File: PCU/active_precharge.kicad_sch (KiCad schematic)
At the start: 0 parts

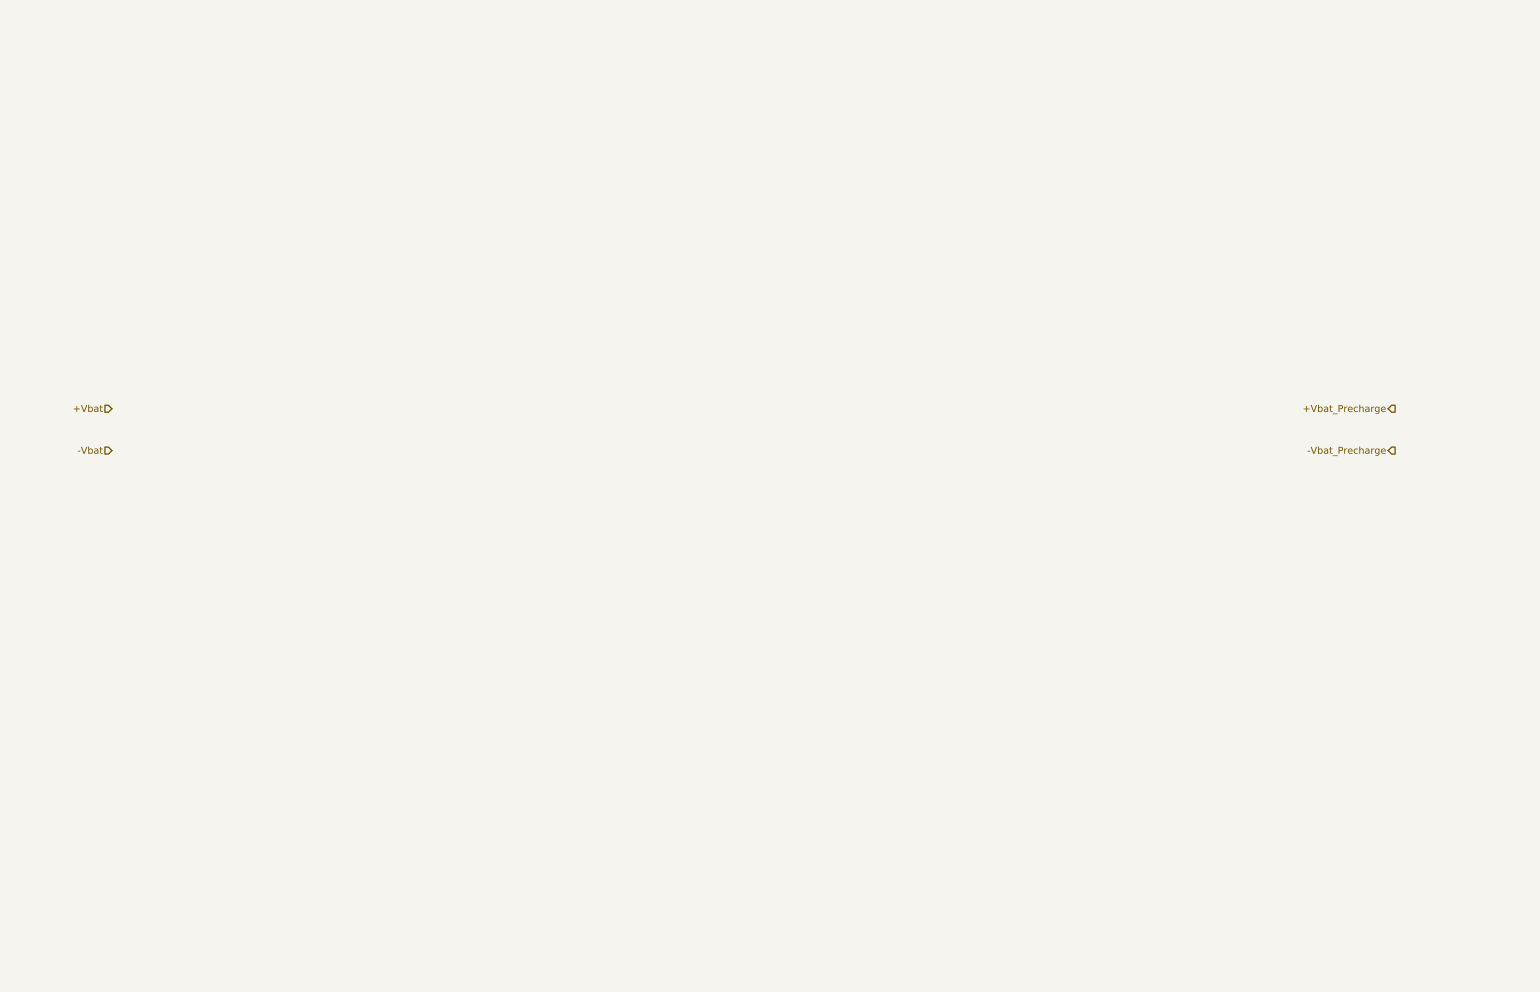
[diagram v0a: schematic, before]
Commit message: Active precharge Block
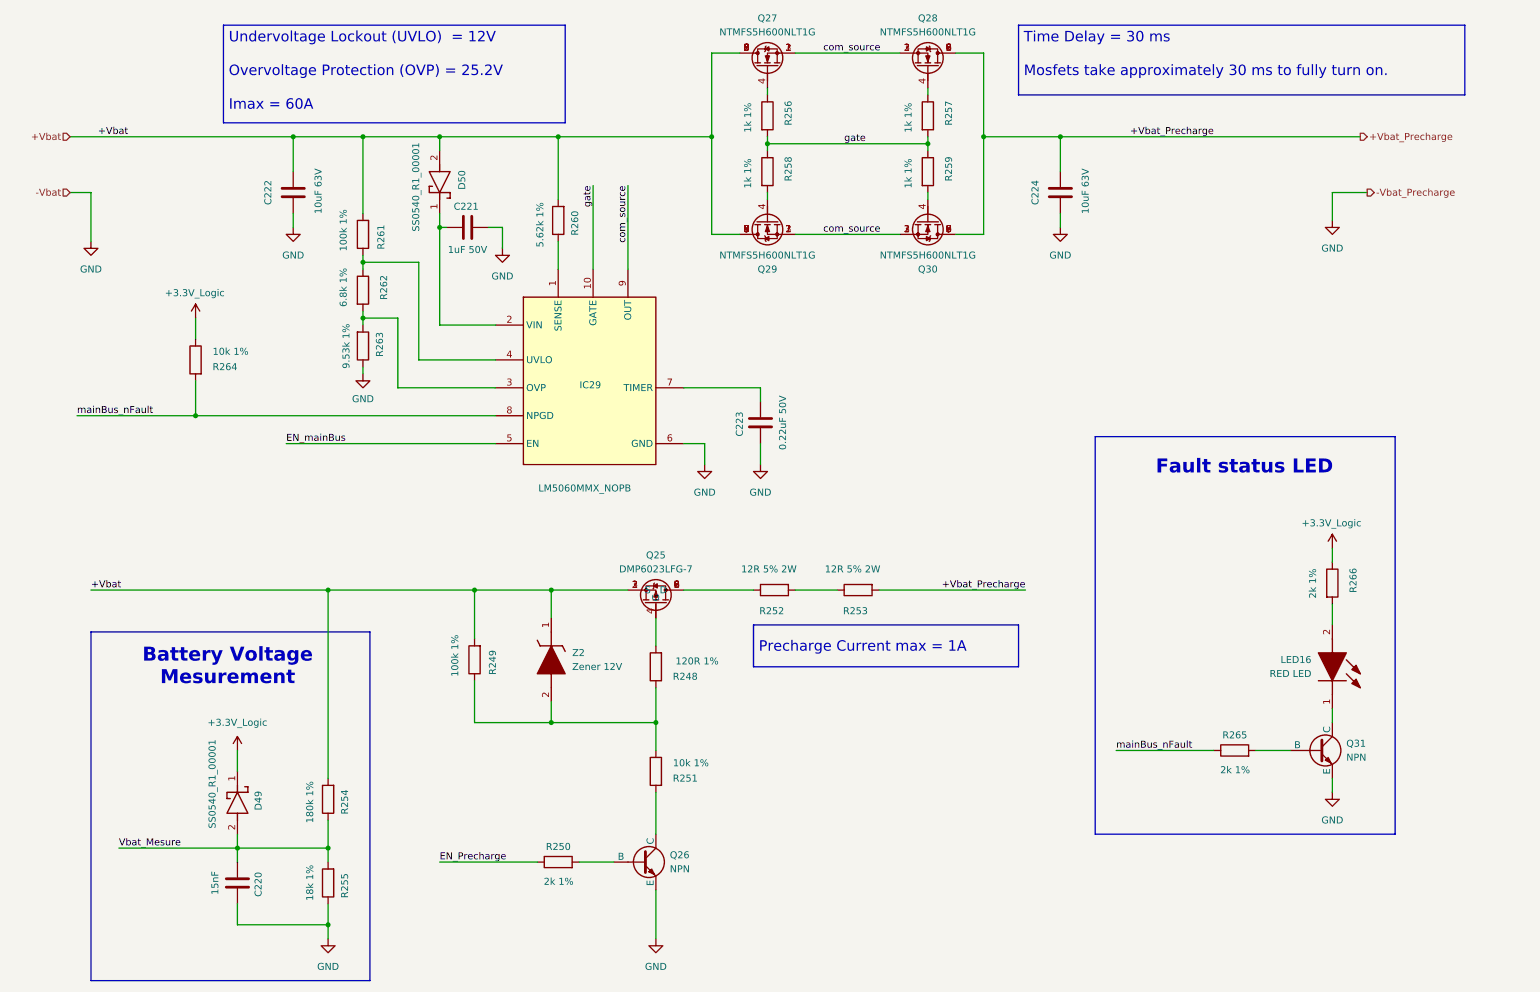
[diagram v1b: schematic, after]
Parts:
- added C220: 15nF, Capacitor_SMD:C_0603_1608Metric, symbol Device:C
- added C221: 1uF 50V, Capacitor_SMD:C_0805_2012Metric, symbol Device:C
- added C222, C224: 10uF 63V, Capacitor_SMD:C_1210_3225Metric, symbol Device:C
- added C223: 0.22uF 50V, Capacitor_SMD:C_0603_1608Metric, symbol Device:C
- added D49, D50: SS0540_R1_00001, BassingaLib_Diodes:SOD3816X135N, symbol BassingaLib_Diodes:SS0540_R1_00001
- added IC29: LM5060MMX_NOPB, BassingaLib_Gate_Drivers:SOP50P490X110-10N, symbol BassingaLib_Gate_Drivers:LM5060MMX_NOPB
- added LED16: RED LED, BassinaLib_LEDs:LEDM168X80N, symbol BassinaLib_LEDs:APHD1608LSURCK
- added Q25: DMP6023LFG-7, BassingaLib_Mosfets:DMP4013LFG7, symbol BassingaLib_Mosfets:DMP6023LFG-7
- added Q26, Q31: NPN, Package_TO_SOT_SMD:SOT-23, symbol Simulation_SPICE:NPN
- added Q27, Q28, Q29, Q30: NTMFS5H600NLT1G, BassingaLib_Mosfets:NTMFS5H600NLT1G, symbol BassingaLib_Mosfets:NTMFS5H600NLT1G
- added R248: 120R 1%, Resistor_SMD:R_0603_1608Metric, symbol Device:R
- added R249, R261: 100k 1%, Resistor_SMD:R_0603_1608Metric, symbol Device:R
- added R250, R265, R266: 2k 1%, Resistor_SMD:R_0603_1608Metric, symbol Device:R
- added R251, R264: 10k 1%, Resistor_SMD:R_0603_1608Metric, symbol Device:R
- added R252, R253: 12R 5% 2W, Resistor_SMD:R_2512_6332Metric, symbol Device:R
- added R254: 180k 1%, Resistor_SMD:R_0603_1608Metric, symbol Device:R
- added R255: 18k 1%, Resistor_SMD:R_0603_1608Metric, symbol Device:R
- added R256, R257, R258, R259: 1k 1%, Resistor_SMD:R_0603_1608Metric, symbol Device:R
- added R260: 5.62k 1%, Resistor_SMD:R_0603_1608Metric, symbol Device:R
- added R262: 6.8k 1%, Resistor_SMD:R_0603_1608Metric, symbol Device:R
- added R263: 9.53k 1%, Resistor_SMD:R_0603_1608Metric, symbol Device:R
- added Z2: Zener 12V, BassingaLib_Zener_Diodes:SOD3716X135N, symbol BassingaLib_Zener_Diodes:MMSZ12T1G
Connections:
- net +Vbat: now also C222.2, D50.2 (A), Q25.1 (S), Q25.2 (S), Q25.3 (S), Q27.5, Q27.6, Q27.7, Q27.8, Q27.9, Q29.5, Q29.6, Q29.7, Q29.8, Q29.9, R249.2, R254.2, R260.2, R261.2, Z2.1 (K)
- net +Vbat_Precharge: now also C224.2, Q28.5, Q28.6, Q28.7, Q28.8, Q28.9, Q30.5, Q30.6, Q30.7, Q30.8, Q30.9, R253.2
- new net: C221.1, D50.1 (K), IC29.2 (VIN)
- new net: R252.2, R253.1
- new net: LED16.2 (A), R266.2
- new net: Q30.4, R259.2
- new net: Q25.5 (D), Q25.6 (D), Q25.7 (D), Q25.8 (D), Q25.9 (D), R252.1
- new net: Q26.2 (B), R250.2
- new net: IC29.4 (UVLO), R261.1, R262.1
- new net: IC29.3 (OVP), R262.2, R263.2
- new net: R248.1, R249.1, R251.1, Z2.2 (A)
- new net: Q28.4, R257.1
- new net: Q29.4, R258.2
- new net: LED16.1 (K), Q31.1 (C)
- new net: Q25.4 (G), R248.2
- new net: Q31.2 (B), R265.2
- new net: C223.2, IC29.7 (TIMER)
- new net: Q26.1 (C), R251.2
- new net: IC29.1 (SENSE), R260.1
- new net: Q27.4, R256.1
- new net +3.3V_Logic: D49.1 (K), R264.1, R266.1
- new net EN_Precharge: R250.1
- new net EN_mainBus: IC29.5 (EN)
- new net GND: C220.1, C221.2, C222.1, C223.1, C224.1, IC29.6 (GND), Q26.3 (E), Q31.3 (E), R255.1, R263.1
- new net Vbat_Mesure: C220.2, D49.2 (A), R254.1, R255.2
- new net com_source: IC29.9 (OUT), Q27.1, Q27.2, Q27.3, Q28.1, Q28.2, Q28.3, Q29.1, Q29.2, Q29.3, Q30.1, Q30.2, Q30.3
- new net gate: IC29.10 (GATE), R256.2, R257.2, R258.1, R259.1
- new net mainBus_nFault: IC29.8 (NPGD), R264.2, R265.1
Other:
- note added: "Battery Voltage Mesurement"
- note added: "Fault status LED"

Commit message: Logic PSU Completed
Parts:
- removed C220: 15nF, Capacitor_SMD:C_0603_1608Metric, symbol Device:C
- removed D49: SS0540_R1_00001, BassingaLib_Diodes:SOD3816X135N, symbol BassingaLib_Diodes:SS0540_R1_00001
- removed R254: 180k 1%, Resistor_SMD:R_0603_1608Metric, symbol Device:R
- removed R255: 18k 1%, Resistor_SMD:R_0603_1608Metric, symbol Device:R
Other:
- note removed: "Battery Voltage Mesurement"

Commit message: Supervisor Block
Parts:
- removed Q26, Q31: NPN, Package_TO_SOT_SMD:SOT-23, symbol Simulation_SPICE:NPN
- added Q21, Q27: Q_NPN, Package_TO_SOT_SMD:SOT-23, symbol Device:Q_NPN
- renumbered C222 to C193, C221 to C196, C223 to C199, C224 to C203, D50 to D44, IC29 to IC32, Q25 to Q22, Q27 to Q23, Q29 to Q24, Q28 to Q25, Q30 to Q26, R264 to R207, R261 to R214, R262 to R215, R263 to R216, R249 to R220, R260 to R221, R250 to R222, R248 to R225, R251 to R226, R256 to R227, R258 to R228, R252 to R229, R253 to R230, R257 to R232, R259 to R233, R265 to R235, R266 to R236, Z2 to Z1
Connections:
- net GND: now also Q21.E, Q27.E
- net at R222.2: now also Q21.B
- net at LED16.1 (K): now also Q27.C
- net at R235.2: now also Q27.B
- net at R226.2: now also Q21.C
- net +Vbat_Precharge renamed +Vbus
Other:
- moved on the sheet: LED16, R235, R236

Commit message: Start of PCB Design
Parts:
- removed Q21, Q27: Q_NPN, Package_TO_SOT_SMD:SOT-23, symbol Device:Q_NPN
- added Q21, Q27: BC846B, BassingaLib_BJT:SOT95P230X110-3N, symbol BassingaLib_BJT:BC846B
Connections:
- net GND: now also Q21.2 (E), Q27.2 (E)
- net at R222.2: now also Q21.1 (B)
- net at LED16.1 (K): now also Q27.3 (C)
- net at R235.2: now also Q27.1 (B)
- net at R226.2: now also Q21.3 (C)
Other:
- moved on the sheet: LED16, R235, R236

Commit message: PCB Design started
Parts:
- R214: value 100k 1% -> 91k 1%; Manufacturer_Part_Number AT0603FRE07100KL -> RT0603BRD0791KL
- R215: value 6.8k 1% -> 10k 1%; Manufacturer_Part_Number AC0603FR-076K8L -> AF0603FR-0710KL
- R216: value 9.53k 1% -> 8k 1%; Manufacturer_Part_Number AF0603FR-079K53L -> RT0603BRE078KL
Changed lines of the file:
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@@
 		)
 	)
-	(text_box "Undervoltage Lockout (UVLO)  = 12V\n\nOvervoltage Protection (OVP) = 25.2V\n\nImax = 60A"
+	(text_box "Undervoltage Lockout (UVLO)  = 10V\n\nOvervoltage Protection (OVP) = 28V\n\nImax = 60A"
 		(exclude_from_sim no)
 		(at 53.34 17.78 0)
@@
 	(symbol
 		(lib_id "Device:R")
+		(at 78.74 66.04 0)
+		(mirror y)
+		(unit 1)
+		(exclude_from_sim no)
+		(in_bom yes)
+		(on_board yes)
+		(dnp no)
+		(property "Reference" "R215"
+			(at 86.36 67.31 0)
+			(effects
+				(font
+					(size 1.27 1.27)
+				)
+				(justify left)
+			)
+		)
+		(property "Value" "10k 1%"
+			(at 88.392 64.516 0)
+			(effects
+				(font
+					(size 1.27 1.27)
+				)
+				(justify left)
+			)
+		)
+		(property "Footprint" "Resistor_SMD:R_0603_1608Metric"
+			(at 80.518 66.04 90)
+			(effects
+				(font
+					(size 1.27 1.27)
+				)
+				(hide yes)
+			)
+		)
+		(property "Datasheet" "~"
+			(at 78.74 66.04 0)
+			(effects
+				(font
+					(size 1.27 1.27)
+				)
+				(hide yes)
+			)
+		)
+		(property "Description" "Resistor"
+			(at 78.74 66.04 0)
+			(effects
+				(font
+					(size 1.27 1.27)
+				)
+				(hide yes)
+			)
+		)
+		(property "Manufacturer_Name" "YAGEO"
+			(at 78.74 66.04 0)
+			(effects
+				(font
+					(size 1.27 1.27)
+				)
+				(hide yes)
+			)
+		)
+		(property "Manufacturer_Part_Number" "AF0603FR-0710KL"
+			(at 78.74 66.04 0)
+			(effects
+				(font
+					(size 1.27 1.27)
+				)
+				(hide yes)
+			)
+		)
+		(property "Packaging" "0603 (608mm)"
+			(at 78.74 66.04 0)
+			(effects
+				(font
+					(size 1.27 1.27)
+				)
+				(hide yes)
+			)
+		)
+		(pin "1"
+		)
+		(pin "2"
+		)
+		(instances
+			(project "PCU"
+				(path "/c5277b98-916c-45ac-b199-6b9ee16008ba/0aad7a0a-408b-4596-959e-c6df745f73d1"
+					(reference "R215")
+					(unit 1)
+				)
+			)
+		)
+	)
+	(symbol
+		(lib_id "Device:R")
 		(at 168.91 120.65 90)
 		(mirror x)
@@
 	(symbol
 		(lib_id "Device:R")
-		(at 78.74 66.04 0)
-		(unit 1)
-		(exclude_from_sim no)
-		(in_bom yes)
-		(on_board yes)
-		(dnp no)
-		(property "Reference" "R215"
-			(at 82.55 67.818 90)
-			(effects
-				(font
-					(size 1.27 1.27)
-				)
-				(justify left)
-			)
-		)
-		(property "Value" "6.8k 1%"
-			(at 75.184 69.088 90)
-			(effects
-				(font
-					(size 1.27 1.27)
-				)
-				(justify left)
-			)
-		)
-		(property "Footprint" "Resistor_SMD:R_0603_1608Metric"
-			(at 76.962 66.04 90)
-			(effects
-				(font
-					(size 1.27 1.27)
-				)
-				(hide yes)
-			)
-		)
-		(property "Datasheet" "~"
-			(at 78.74 66.04 0)
-			(effects
-				(font
-					(size 1.27 1.27)
-				)
-				(hide yes)
-			)
-		)
-		(property "Description" "Resistor"
-			(at 78.74 66.04 0)
-			(effects
-				(font
-					(size 1.27 1.27)
-				)
-				(hide yes)
-			)
-		)
-		(property "Manufacturer_Name" "YAGEO"
-			(at 78.74 66.04 0)
-			(effects
-				(font
-					(size 1.27 1.27)
-				)
-				(hide yes)
-			)
-		)
-		(property "Manufacturer_Part_Number" "AC0603FR-076K8L"
-			(at 78.74 66.04 0)
-			(effects
-				(font
-					(size 1.27 1.27)
-				)
-				(hide yes)
-			)
-		)
-		(property "Packaging" "0603 (608mm)"
-			(at 78.74 66.04 0)
-			(effects
-				(font
-					(size 1.27 1.27)
-				)
-				(hide yes)
-			)
-		)
-		(pin "1"
-		)
-		(pin "2"
-		)
-		(instances
-			(project "PCU"
-				(path "/c5277b98-916c-45ac-b199-6b9ee16008ba/0aad7a0a-408b-4596-959e-c6df745f73d1"
-					(reference "R215")
-					(unit 1)
-				)
-			)
-		)
-	)
-	(symbol
-		(lib_id "Device:R")
 		(at 99.06 133.35 180)
 		(unit 1)
@@
 			)
 		)
-		(property "Value" "100k 1%"
+		(property "Value" "91k 1%"
 			(at 75.184 51.308 90)
 			(effects
@@
 			)
 		)
-		(property "Manufacturer_Part_Number" "AT0603FRE07100KL"
+		(property "Manufacturer_Part_Number" "RT0603BRD0791KL"
 			(at 78.74 55.88 0)
 			(effects
@@
 			)
 		)
-		(property "Value" "9.53k 1%"
+		(property "Value" "8k 1%"
 			(at 75.692 72.136 90)
 			(effects
@@
 			)
 		)
-		(property "Manufacturer_Part_Number" "AF0603FR-079K53L"
+		(property "Manufacturer_Part_Number" "RT0603BRE078KL"
 			(at 78.74 76.2 0)
 			(effects

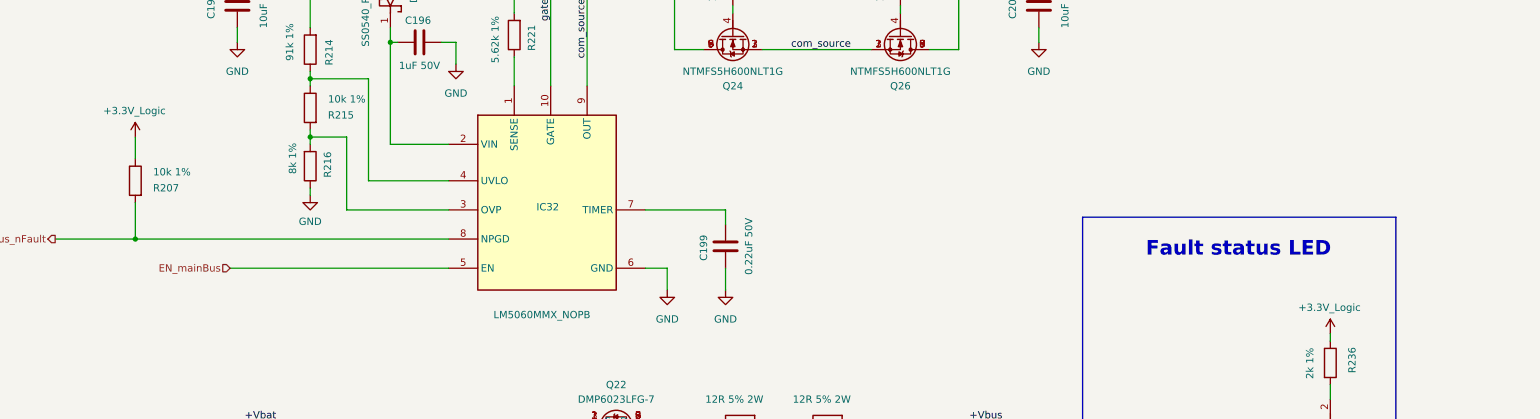
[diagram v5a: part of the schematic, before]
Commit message: PSU Blocks Routed
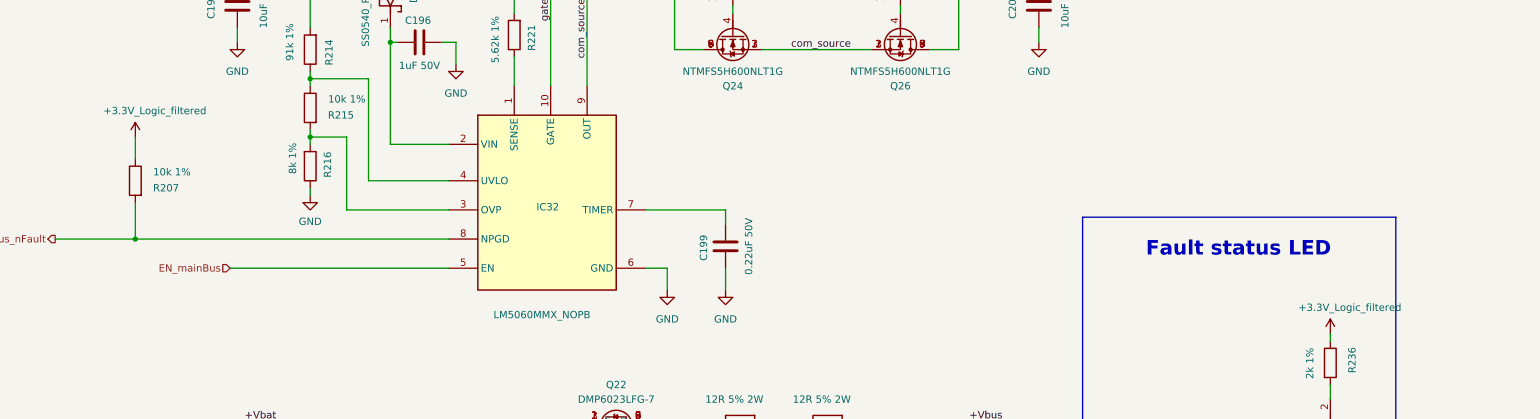
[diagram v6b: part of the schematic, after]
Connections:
- net +3.3V_Logic renamed +3.3V_Logic_filtered
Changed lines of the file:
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@@
 			)
 		)
-		(property "Value" "+3.3V_Logic"
+		(property "Value" "+3.3V_Logic_filtered"
 			(at 250.952 100.838 0)
 			(effects
@@
 			)
 		)
-		(property "Value" "+3.3V_Logic"
+		(property "Value" "+3.3V_Logic_filtered"
 			(at 42.672 66.548 0)
 			(effects

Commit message: Fly controller design started
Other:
- company: BASSINGA Lab -> BASSINGA_LAB
- title: (none) -> Propulsion Control Unit
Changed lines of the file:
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@@
 	(paper "A4")
 	(title_block
+		(title "Propulsion Control Unit")
 		(date "2025-05-21")
 		(rev "v1.0")
-		(company "BASSINGA Lab")
+		(company "BASSINGA_LAB")
+		(comment 1 "Copyright © 2025 Andresse Brisel BASSINGA ")
 	)
 	(rectangle
